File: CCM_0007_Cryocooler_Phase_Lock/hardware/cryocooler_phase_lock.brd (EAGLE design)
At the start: 63.5 x 101.6 mm, 33 parts, among them Q1 CMA-4544PF-W, U1 MAX4466EXK+T, U3 PHOTON_WITH_HEADERS, X1 22-23-2021, X2 22-23-2021, X3 BNC_VERTICAL, X4 BNC_VERTICAL, X5 BNC_VERTICAL, X6 BNC_VERTICAL

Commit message: CCM_0007: finished initial board layout.
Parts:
- moved D1 275.8 mm to (60.2, 30.5)
- moved X3 269.1 mm to (74.9, 24.1), flipped to the bottom
- moved R9 254.3 mm to (64.1, 12.7)
- moved R8 251.3 mm to (64.0, 29.8), turned to 180 degrees
- moved R7 250.1 mm to (64.0, 31.8)
- moved R12 245.5 mm to (12.1, 31.8)
- moved R11 226.8 mm to (12.1, 12.7)
- moved X6 224.4 mm to (1.27, 39.4), flipped to the bottom, turned to 180 degrees
- moved X5 191.5 mm to (1.27, 20.3), flipped to the bottom, turned to 180 degrees
- moved C10 187.9 mm to (53.1, 32.5), turned to 180 degrees
- moved C11 186.3 mm to (53.2, 34.5)
- moved Q1 170.8 mm to (38.1, 40.6)
- moved C7 158.0 mm to (39.4, 25.3), turned to 90 degrees
- moved R10 156.2 mm to (41.3, 25.3), turned to 90 degrees
- moved C5 155.5 mm to (46.4, 32.8), turned to 90 degrees
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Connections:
- net N$11 renamed SYNC_OUT
- net N$13 renamed TRIGGER_OUT
- net N$8 renamed VOLUME_INDICATOR
- removed net N$7: R7.2, X3.SIGNAL
- new net N10: D1.3, R7.1, R8.2, U3.11
- net DELAY_ADJUST: now also R7.2, X3.SIGNAL; no longer D1.3, R7.1, R8.2, U3.11
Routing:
- net N$12: track 0.00 -> 30.1 mm
- net GND: track 2.34 -> 30.5 mm, vias 0 -> 10
- net N$10: track 0.00 -> 27.1 mm
- net N$1: track 0.00 -> 13.4 mm
- net AUDIO_IN: track 0.00 -> 6.34 mm
- net N$3: track 0.00 -> 5.70 mm
- net N$2: track 0.00 -> 5.55 mm
- net N10: track 0.00 -> 4.90 mm
- net N$5: track 0.00 -> 3.43 mm
- net DELAY_ADJUST: track 0.00 -> 2.41 mm
- net VOLUME_INDICATOR: track 0.00 -> 2.29 mm
- net TRIGGER_OUT: track 0.00 -> 2.29 mm
- net SYNC_OUT: track 0.00 -> 2.29 mm
- net N$6: track 0.00 -> 1.91 mm
- net N$4: track 0.00 -> 1.91 mm
- added copper zone on layer 1, net 3.3V
- removed copper zone on layer 1, net +3.3V
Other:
- board size 63.5 x 101.6 mm -> 76.2 x 47 mm

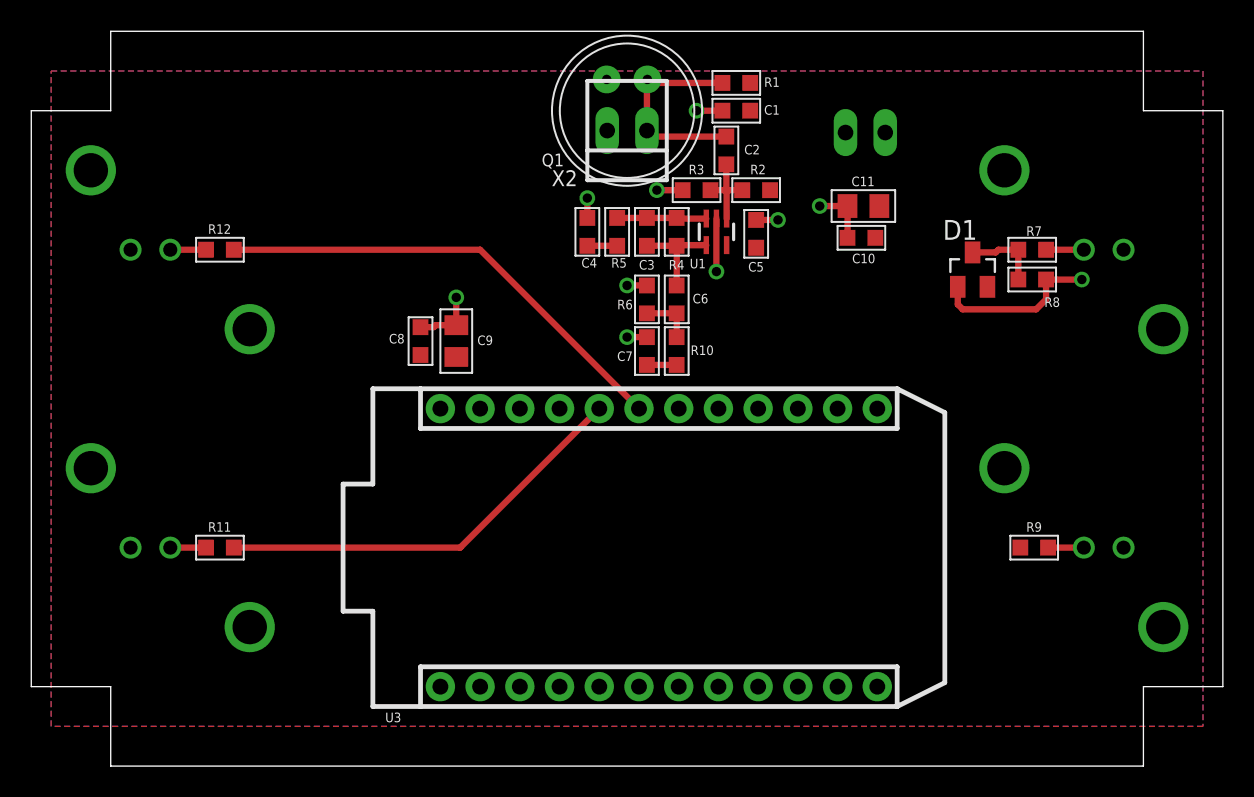
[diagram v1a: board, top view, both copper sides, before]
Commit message: More work on cryocooler interlock, uploaded ordering files.
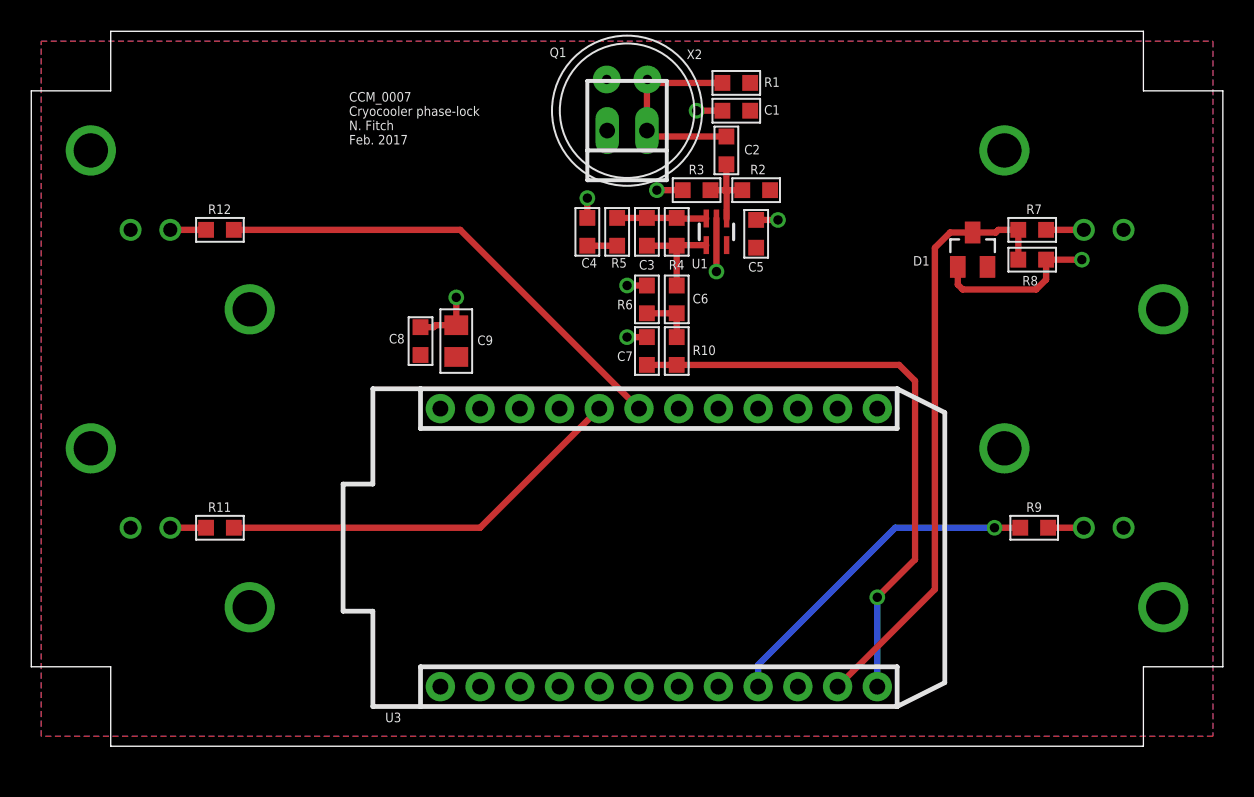
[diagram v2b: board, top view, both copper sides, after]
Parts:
- removed C10: 0.1u, acrooptics:0603
- removed C11: 4.7u, acrooptics:0805
- removed X1: 22-23-2021, con-molex:22-23-2021
- moved R12 1.27 mm to (12.1, 33.0)
- moved R7 1.27 mm to (64.0, 33.0)
- moved X6 1.27 mm to (1.27, 40.6)
- moved R11 1.27 mm to (12.1, 14.0)
- moved R9 1.27 mm to (64.1, 14.0)
- moved D1 1.27 mm to (60.2, 31.8)
- moved R8 1.27 mm to (64.0, 31.1)
- moved X3 1.27 mm to (74.9, 25.4)
- moved X4 1.27 mm to (74.9, 6.35)
- moved X5 1.27 mm to (1.27, 21.6)
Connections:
- net 3.3V: no longer C10.1, C11.2, X1.1
- net GND: no longer C10.2, C11.1, X1.2
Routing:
- net N$6: track 1.91 -> 38.1 mm, vias 0 -> 1
- net N10: track 4.90 -> 38.4 mm
- net N$9: track 0.00 -> 21.8 mm, vias 0 -> 1
- net GND: track 30.5 -> 26.7 mm, vias 10 -> 9
- net N$12: track 30.1 -> 30.6 mm
- net N$10: track 27.1 -> 26.5 mm
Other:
- board size 76.2 x 47 mm -> 76.2 x 45.7 mm
- board text added: "CCM_0007 Cryocooler phase-lock N. Fitch Feb. 2017"
